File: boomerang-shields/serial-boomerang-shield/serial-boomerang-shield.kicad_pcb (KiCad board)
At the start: 2 copper layers, 78 x 55 mm, 11 parts, among them J1 Power output header, J10 Pin Socket D, J2 USBasp header, J3 Port A, J4 Port B, J5 Port C, J6 Port D, J7 Pin Socket A, J8 Pin Socket B, J9 Pin Socket C

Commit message: Serial Boomerang Shield updated + Gerber files generated
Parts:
- added ?: LOGO, LOGO, F.Cu at (59.4, 17.0)
- added ?: LOGO, LOGO, F.Cu at (37.0, 5.50)
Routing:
- net Net-(J10-Pin_3): track 28.5 -> 23.5 mm
- net Net-(J10-Pin_2): track 30.7 -> 26.1 mm
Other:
- board text added: "2024 B. MARKUS"
- board text added: "AVR-SBC SERIAL USB BOOMERANG SHIELD VER 1.0"
- board text added: "CP2102 Module"

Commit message: Serial Boomerang Shield updated, power output header added
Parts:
- removed the ? at (59.4, 17.0)
- removed the ? at (37.0, 5.50)
- added ?: LOGO, LOGO, F.Cu at (59.4, 16.7)
- added J3: Power output, Connector_PinSocket_2.54mm:PinSocket_2x02_P2.54mm_Vertical, F.Cu at (36.0, 6.61)
- J1: value Power output header -> Power connector to board
- J2: value USBasp header -> USBasp connector to board
- renumbered J9 to J10, J5 to J11, J8 to J4, J4 to J5, J10 to J6, J6 to J7, J7 to J8, J3 to J9
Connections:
- J1 pad 1: unconnected-(J1-Pin_1-Pad1) -> +5V
- J1 pad 3: unconnected-(J1-Pin_3-Pad3) -> +5V
- J1 pad 5: unconnected-(J1-Pin_5-Pad5) -> +5V
- J1 pad 7: unconnected-(J1-Pin_7-Pad7) -> +5V
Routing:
- net +5V: track 0.00 -> 38.7 mm
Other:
- board text added: "Power header"
- board text added: "USBasp header"
- board text removed: "USBasp"

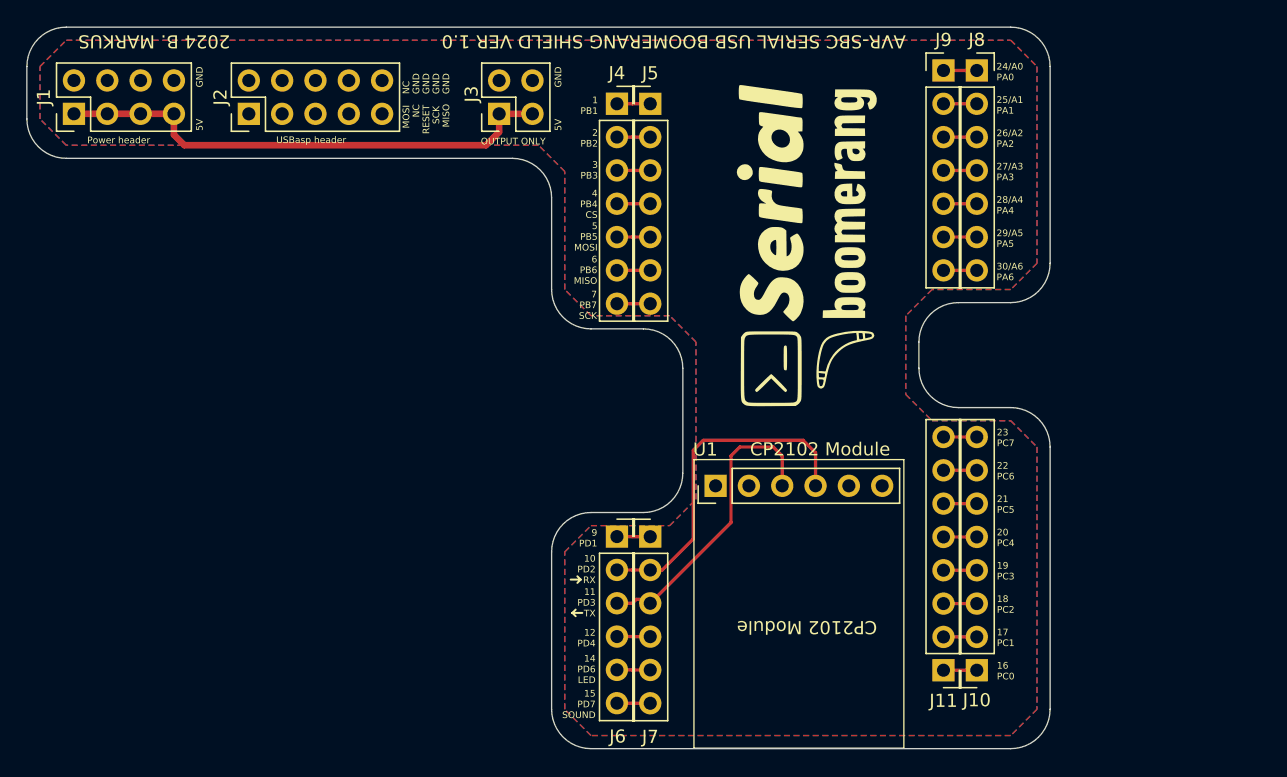
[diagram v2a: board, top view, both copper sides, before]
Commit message: Serial Boomerang Shield updated - Power header realigned to match 0.254mm grid
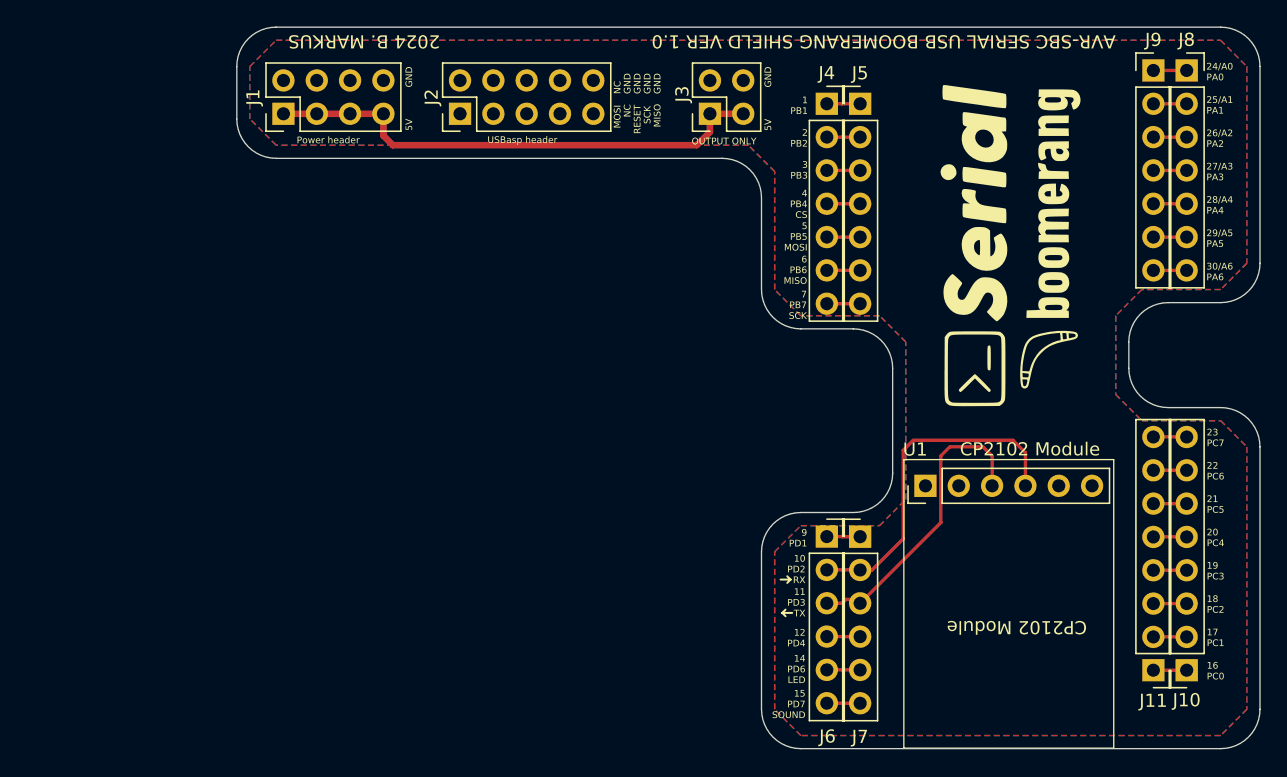
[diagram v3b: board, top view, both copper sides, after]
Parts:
- moved J2 16.1 mm to (33.0, 6.60)
- moved J3 16.1 mm to (52.1, 6.60)
- moved J10 16.0 mm to (88.4, 49.0)
- moved J11 16.0 mm to (85.9, 49.0)
- moved J4 16.0 mm to (61.0, 5.84)
- moved J5 16.0 mm to (63.5, 5.84)
- moved J6 16.0 mm to (61.0, 38.8)
- moved J7 16.0 mm to (63.5, 38.8)
- moved J8 16.0 mm to (88.4, 3.30)
- moved J9 16.0 mm to (85.9, 3.30)
- moved U1 16.0 mm to (82.9, 33.0)
- moved J1 16.0 mm to (19.6, 6.60)
- moved ? 15.5 mm to (74.9, 16.7)

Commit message: Serial Boomerang Shield updated - GPIO headers realigned to match 0.254mm grid
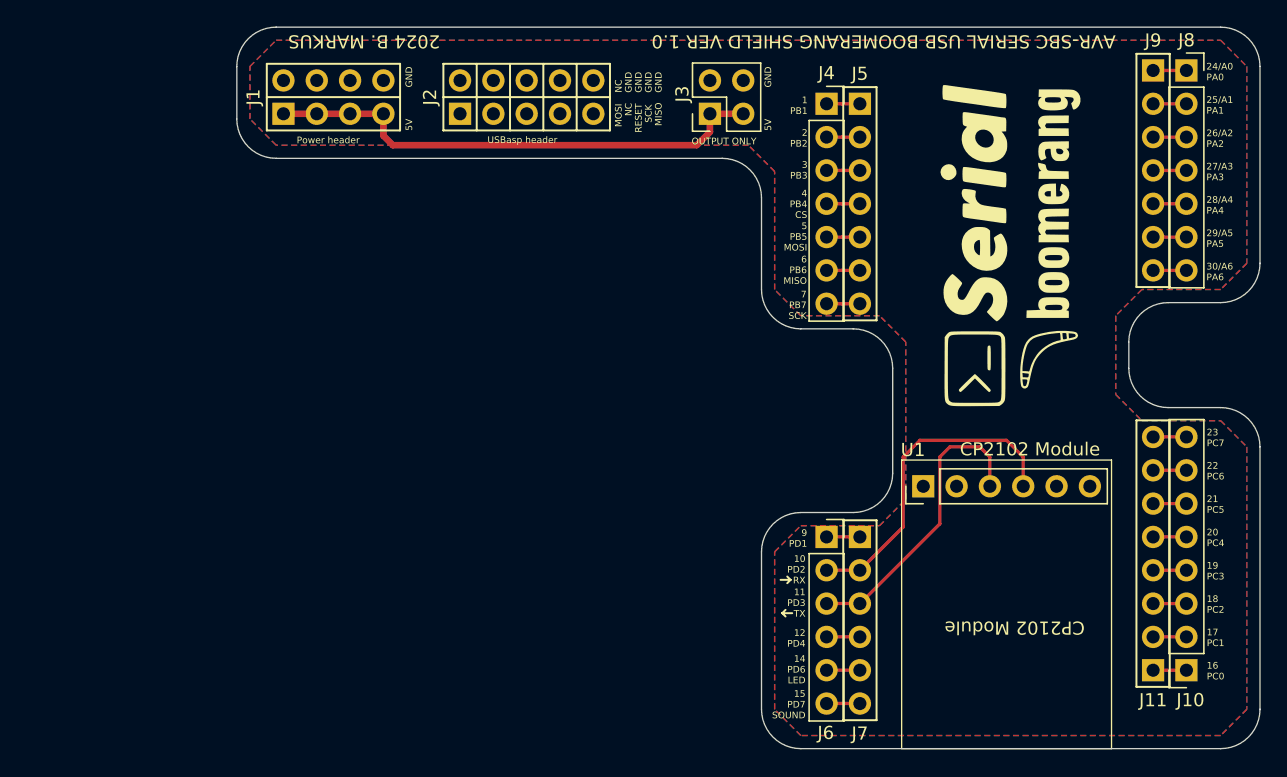
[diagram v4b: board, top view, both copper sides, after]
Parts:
- J1: footprint Connector_PinHeader_2.54mm:PinHeader_2x04_P2.54mm_Vertical -> Connector_PinSocket_2.54mm:PinSocket_2x04_P2.54mm_Vertical; moved to B.Cu
- J11: footprint Connector_PinHeader_2.54mm:PinHeader_1x08_P2.54mm_Vertical -> Connector_PinSocket_2.54mm:PinSocket_1x08_P2.54mm_Vertical; moved to B.Cu
- J2: footprint Connector_PinHeader_2.54mm:PinHeader_2x05_P2.54mm_Vertical -> Connector_PinSocket_2.54mm:PinSocket_2x05_P2.54mm_Vertical; moved to B.Cu
- J5, J9: footprint Connector_PinHeader_2.54mm:PinHeader_1x07_P2.54mm_Vertical -> Connector_PinSocket_2.54mm:PinSocket_1x07_P2.54mm_Vertical; moved to B.Cu
- J7: footprint Connector_PinHeader_2.54mm:PinHeader_1x06_P2.54mm_Vertical -> Connector_PinSocket_2.54mm:PinSocket_1x06_P2.54mm_Vertical; moved to B.Cu
- moved U1 0.17 mm to (82.7, 33.0)
- turned J7 to 180 degrees
- turned J5 to 180 degrees
- turned J11 to 0 degrees
- turned J9 to 180 degrees
- turned J1 to -90 degrees
- turned J2 to -90 degrees
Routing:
- net Net-(J6-Pin_2): track 26.1 -> 25.0 mm
- net Net-(J6-Pin_3): track 23.5 -> 22.9 mm
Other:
- board text added: "J1"
- board text added: "J11"
- board text added: "J2"
- board text added: "J5"
- board text added: "J7"
- board text added: "J9"
